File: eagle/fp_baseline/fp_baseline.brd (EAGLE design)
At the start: 77.6 x 26.6 mm, 6 parts, among them J5 TSM-105-01-S-SV

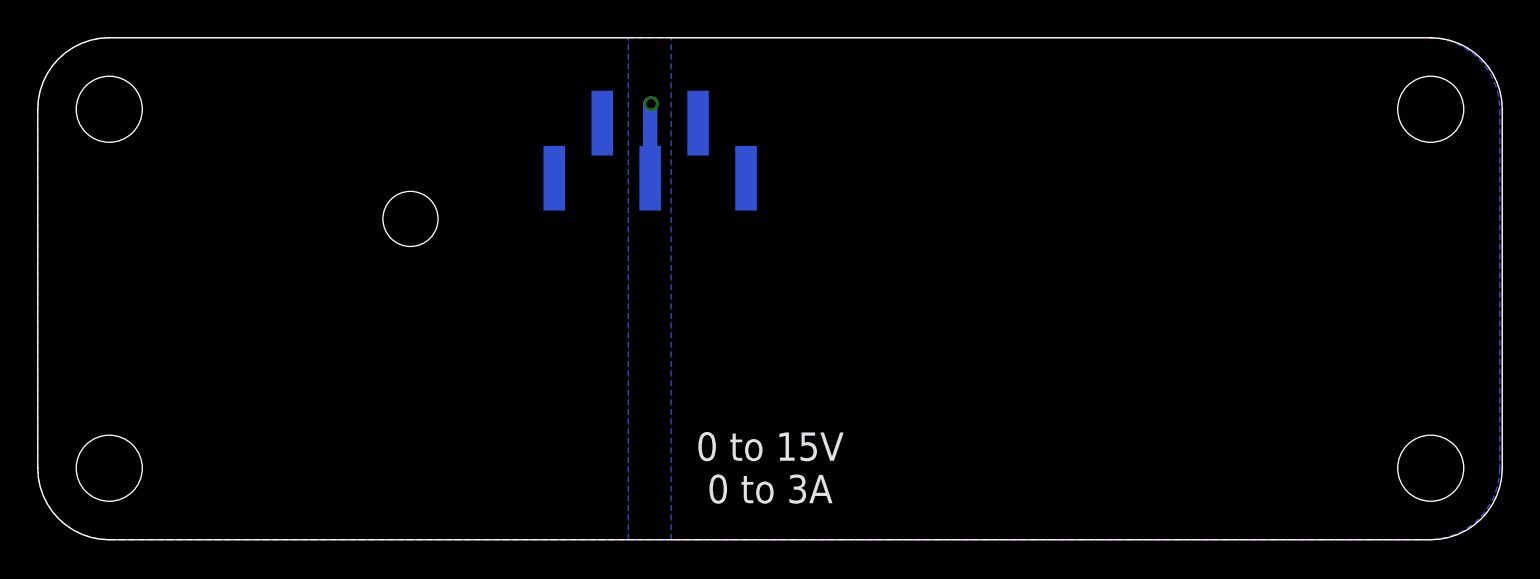
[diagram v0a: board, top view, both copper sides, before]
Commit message: Pre-production update.
* Increased clearances from chassis/enclosure ground.
* Improved text.
* Added gerbers.
* Added USB back panel.
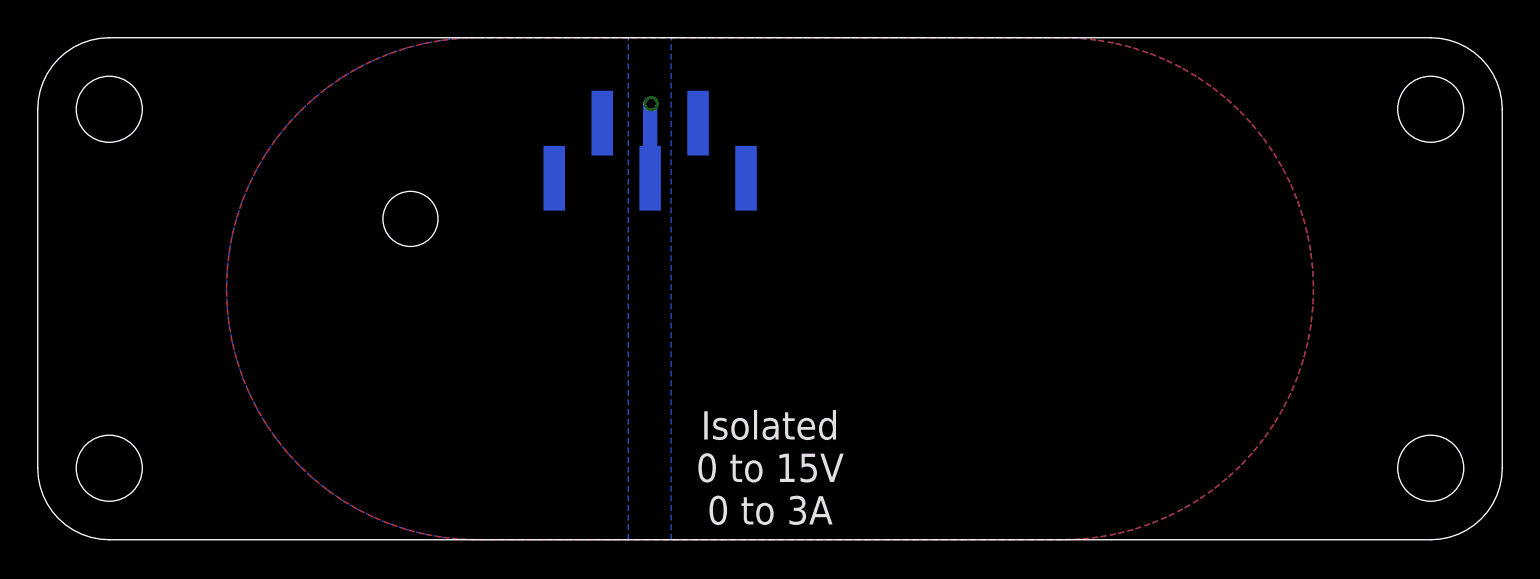
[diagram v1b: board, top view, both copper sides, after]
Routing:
- added copper zone on layer 16, net EXT_IN
- removed copper zone on layer 16, net EXT_NEG
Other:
- board text added: "Isolated 0 to 15V 0 to 3A"
- board text added: "Joulescope Front Panel Reference Baseline Last updated: 2019 Apr 14"
- board text removed: "0 to 15V 0 to 3A"
- board text removed: "Joulescope Front Panel Reference Baseline Last updated: 2019 Mar 20"
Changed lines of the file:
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@@
 <?xml version="1.0" encoding="utf-8"?>
 <!DOCTYPE eagle SYSTEM "eagle.dtd">
-<eagle version="9.3.1">
+<eagle version="9.3.2">
 <drawing>
 <settings>
@@
 <layer number="116" name="Patch_BOT" color="9" fill="4" visible="yes" active="yes"/>
 <layer number="118" name="Rect_Pads" color="7" fill="1" visible="yes" active="yes"/>
-<layer number="121" name="_tsilk" color="7" fill="1" visible="no" active="yes"/>
+<layer number="121" name="_tsilk" color="7" fill="1" visible="yes" active="yes"/>
 <layer number="122" name="_bsilk" color="7" fill="1" visible="yes" active="yes"/>
 <layer number="123" name="tTestmark" color="7" fill="1" visible="yes" active="yes"/>
@@
 <rectangle x1="0" y1="3.78" x2="1.5" y2="22.8" layer="40"/>
 <rectangle x1="76.1" y1="3.78" x2="77.6" y2="22.8" layer="40"/>
-<text x="38.8" y="3.81" size="1.5" layer="121" font="vector" ratio="20" align="center">0 to 15V
+<text x="38.8" y="3.81" size="1.5" layer="121" font="vector" ratio="20" align="center">Isolated
+0 to 15V
 0 to 3A</text>
 <wire x1="0" y1="17.3" x2="16.64" y2="17.3" width="0.254" layer="22"/>
@@
 <dimension x1="0" y1="13.3" x2="19.75" y2="17" x3="-7.5785125" y3="15.15" textsize="1.778" layer="47" dtype="vertical"/>
 <text x="43.18" y="-17.16" size="1.778" layer="153">Joulescope Front Panel Reference Baseline
-Last updated: 2019 Mar 20</text>
+Last updated: 2019 Apr 14</text>
 <text x="17.18" y="-12.86" size="1.778" layer="153">Backside keepout
 (in blue)</text>
@@
 <contactref element="J5" pad="2"/>
 <contactref element="J5" pad="1"/>
-<wire x1="27.37" y1="19.1545" x2="29.91" y2="22.0755" width="0" layer="19" extent="16-16"/>
+<polygon width="0.254" layer="16" thermals="no" rank="3">
+<vertex x="31.29" y="26.6"/>
+<vertex x="23.3" y="26.6" curve="90"/>
+<vertex x="10" y="13.3" curve="90"/>
+<vertex x="23.3" y="0"/>
+<vertex x="31.29" y="0"/>
+</polygon>
 </signal>
 <signal name="EXT_NEG">
 <contactref element="J5" pad="3"/>
-<polygon width="0.1524" layer="1" thermals="no">
-<vertex x="73.81" y="0"/>
-<vertex x="3.79" y="0" curve="-90"/>
-<vertex x="0" y="3.79"/>
-<vertex x="0" y="22.81" curve="-90"/>
-<vertex x="3.79" y="26.6"/>
-<vertex x="73.81" y="26.6" curve="-90"/>
-<vertex x="77.6" y="22.81"/>
-<vertex x="77.6" y="3.79" curve="-90"/>
-</polygon>
-<polygon width="0.254" layer="16" thermals="no" rank="3">
-<vertex x="31.29" y="26.6"/>
-<vertex x="3.79" y="26.6" curve="90"/>
-<vertex x="0" y="22.81"/>
-<vertex x="0" y="3.79" curve="90"/>
-<vertex x="3.79" y="0"/>
-<vertex x="31.29" y="0"/>
+<polygon width="0.254" layer="1" thermals="no">
+<vertex x="23.3" y="26.6"/>
+<vertex x="54.3" y="26.6" curve="-90"/>
+<vertex x="67.6" y="13.3" curve="-90"/>
+<vertex x="54.3" y="0"/>
+<vertex x="23.3" y="0" curve="-90"/>
+<vertex x="10" y="13.3" curve="-90"/>
 </polygon>
 <wire x1="32.45" y1="19.1545" x2="32.45" y2="23.05" width="0.762" layer="16"/>
@@
 <polygon width="0.254" layer="16" isolate="0.254" thermals="no">
 <vertex x="33.56" y="26.6"/>
-<vertex x="73.68" y="26.6" curve="-90"/>
-<vertex x="77.47" y="22.81"/>
-<vertex x="77.47" y="3.79" curve="-90"/>
-<vertex x="73.68" y="0"/>
+<vertex x="54.3" y="26.6" curve="-90"/>
+<vertex x="67.6" y="13.3" curve="-90"/>
+<vertex x="54.3" y="0"/>
 <vertex x="33.56" y="0"/>
 </polygon>
-<wire x1="34.99" y1="22.0755" x2="37.53" y2="19.1545" width="0" layer="19" extent="16-16"/>
 </signal>
 </signals>
